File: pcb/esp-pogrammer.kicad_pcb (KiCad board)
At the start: 2 copper layers, 30.2 x 43.7 mm, 31 parts, among them J1 USB_C_Receptacle_USB2.0, J2 TC2030-IDC, Q1 MMDT3904, Q2 MMDT3904, SW1 SW_SPDT, SW2 SW_Push, SW3 SW_Push, U1 CH340G, U2 AMS1117-3.3, Y1 12 MHz

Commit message: updates layout
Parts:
- moved C5 6.84 mm to (88.6, 57.9)
- moved R2 4.63 mm to (90.7, 53.0)
- moved R5 2.57 mm to (74.4, 73.0), turned to -90 degrees
- moved R1 1.74 mm to (93.0, 53.0)
- moved J2 0.30 mm to (93.7, 73.0)
- moved D1 0.20 mm to (80.3, 72.8)
- moved D2 0.20 mm to (80.3, 76.4)
- moved D3 0.20 mm to (80.3, 80.4)
- moved R6 0.20 mm to (85.8, 72.9), turned to 180 degrees
- moved R7 0.20 mm to (85.8, 76.4), turned to 180 degrees
- moved R8 0.20 mm to (85.8, 80.4), turned to 180 degrees
- turned R9 to 0 degrees
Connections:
- C8 pad 2: Net-(C8-Pad2) -> GND
- R5 pad 1: +3V3 -> 3.3V OUT
- SW2 pad 1: Net-(C8-Pad2) -> GND
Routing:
- net TXD: track 0.00 -> 21.7 mm
- net 3.3V OUT: track 0.00 -> 21.4 mm, vias 0 -> 1
- net VBUS: track 0.00 -> 20.6 mm
- net +3V3: track 0.00 -> 20.3 mm, vias 0 -> 3
- net unconnected-(J1-PadS1): track 0.00 -> 17.0 mm
- net RXD: track 0.00 -> 14.3 mm
- net D+: track 0.00 -> 11.0 mm
- net Net-(J1-PadA5): track 0.00 -> 10.4 mm
- net D-: track 0.00 -> 9.77 mm
- net GND: track 0.00 -> 5.66 mm
- net Net-(D1-Pad2): track 0.00 -> 3.93 mm
- net Net-(D3-Pad2): track 0.00 -> 3.91 mm
- net Net-(D2-Pad2): track 0.00 -> 3.89 mm
- net Net-(D4-Pad2): track 0.00 -> 2.29 mm
- net Net-(J1-PadB5): track 0.00 -> 2.16 mm, vias 0 -> 1
- added copper zone on B.Cu, net +3V3
- added copper zone on F.Cu, net GND

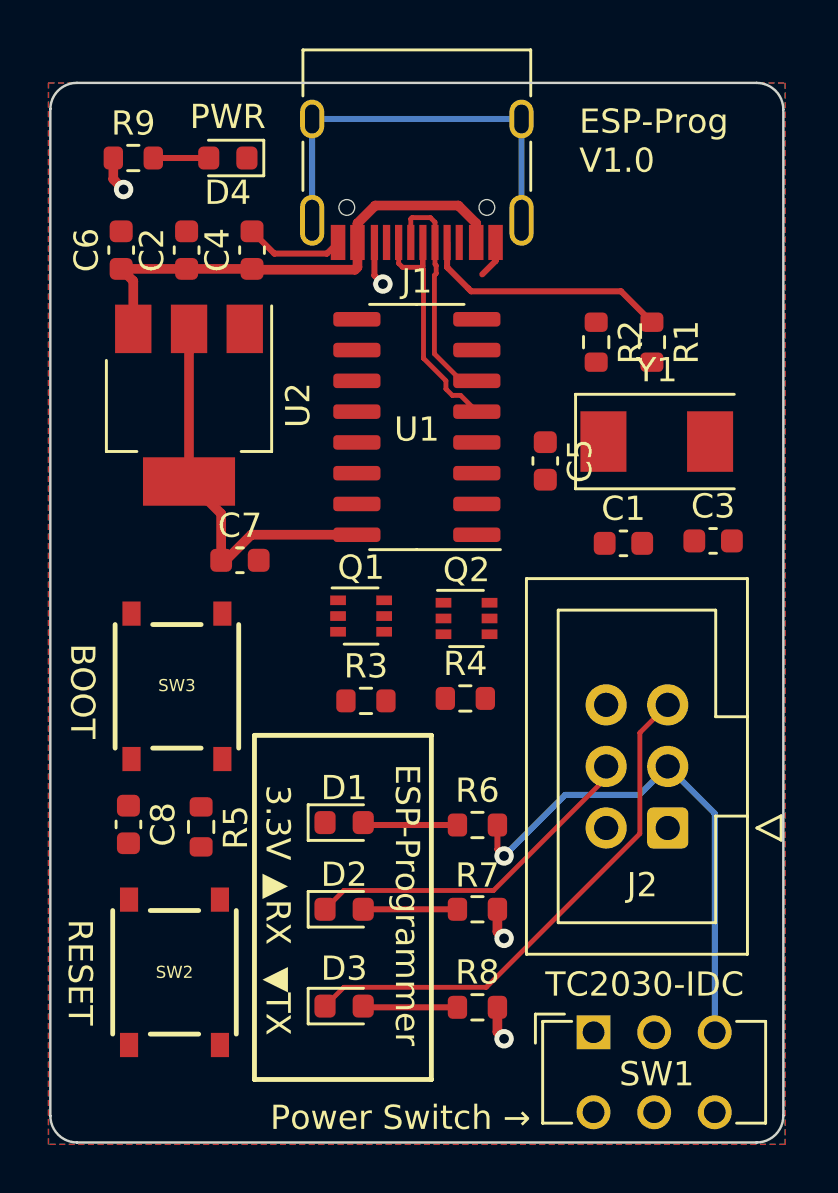
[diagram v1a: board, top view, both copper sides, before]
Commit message: added some filter caps, replaced local chip filter, replaced crystal caps, fixed switched power on reset, routed, rounded.
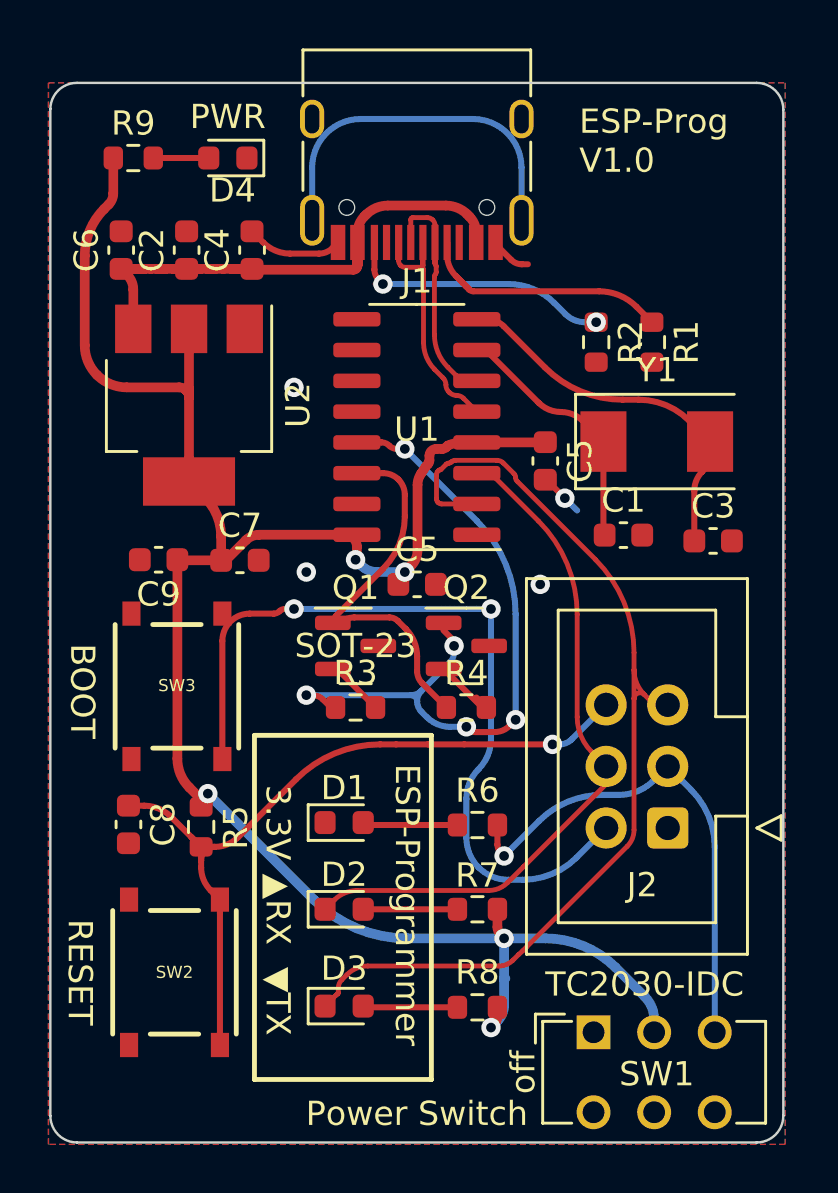
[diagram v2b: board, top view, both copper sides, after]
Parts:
- added C5: 0.1uF, Capacitor_SMD:C_0603_1608Metric, F.Cu at (83.3, 63.0)
- added C9: 10uF, Capacitor_SMD:C_0603_1608Metric, F.Cu at (72.6, 62.0)
- C1, C3: value 10uF -> 22pF
- Q1, Q2: footprint Package_TO_SOT_SMD:SOT-363_SC-70-6 -> Package_TO_SOT_SMD:SOT-23
- moved Q1 1.25 mm to (80.8, 65.5)
- moved Q2 1.13 mm to (85.3, 65.5)
- moved R3 0.51 mm to (80.8, 68.1)
- moved R4 0.37 mm to (85.3, 68.1)
- moved C1 0.34 mm to (91.8, 61.0)
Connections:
- R5 pad 1: 3.3V OUT -> +3V3
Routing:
- net +3V3: track 20.3 -> 85.1 mm, vias 3 -> 5
- net BOOT: track 0.00 -> 33.8 mm, vias 0 -> 2
- net RESET: track 0.00 -> 32.1 mm, vias 0 -> 1
- net DTR: track 0.00 -> 29.9 mm, vias 0 -> 5
- net TXD: track 21.7 -> 41.8 mm
- net RTS: track 0.00 -> 16.1 mm
- net Net-(C3-Pad1): track 0.00 -> 15.5 mm
- net RXD: track 14.3 -> 28.7 mm
- net Net-(C1-Pad1): track 0.00 -> 10.4 mm
- net Net-(J1-PadB5): track 2.16 -> 11.4 mm, vias 1 -> 2
- net Net-(Q2-Pad2): track 0.00 -> 2.90 mm
- net Net-(Q1-Pad2): track 0.00 -> 2.41 mm
- net GND: track 5.66 -> 7.56 mm, vias 0 -> 4
- net unconnected-(J1-PadS1): track 17.0 -> 15.1 mm
- net D+: track 11.0 -> 9.86 mm
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- added copper zone on B.Cu, net GND
- removed copper zone on B.Cu, net +3V3
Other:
- board text added: "Power Switch"
- board text added: "off"
- board text added: "on"
- board text removed: "Power Switch →"

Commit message: fixed transistors. minor changes. ordered prototype 0.1.
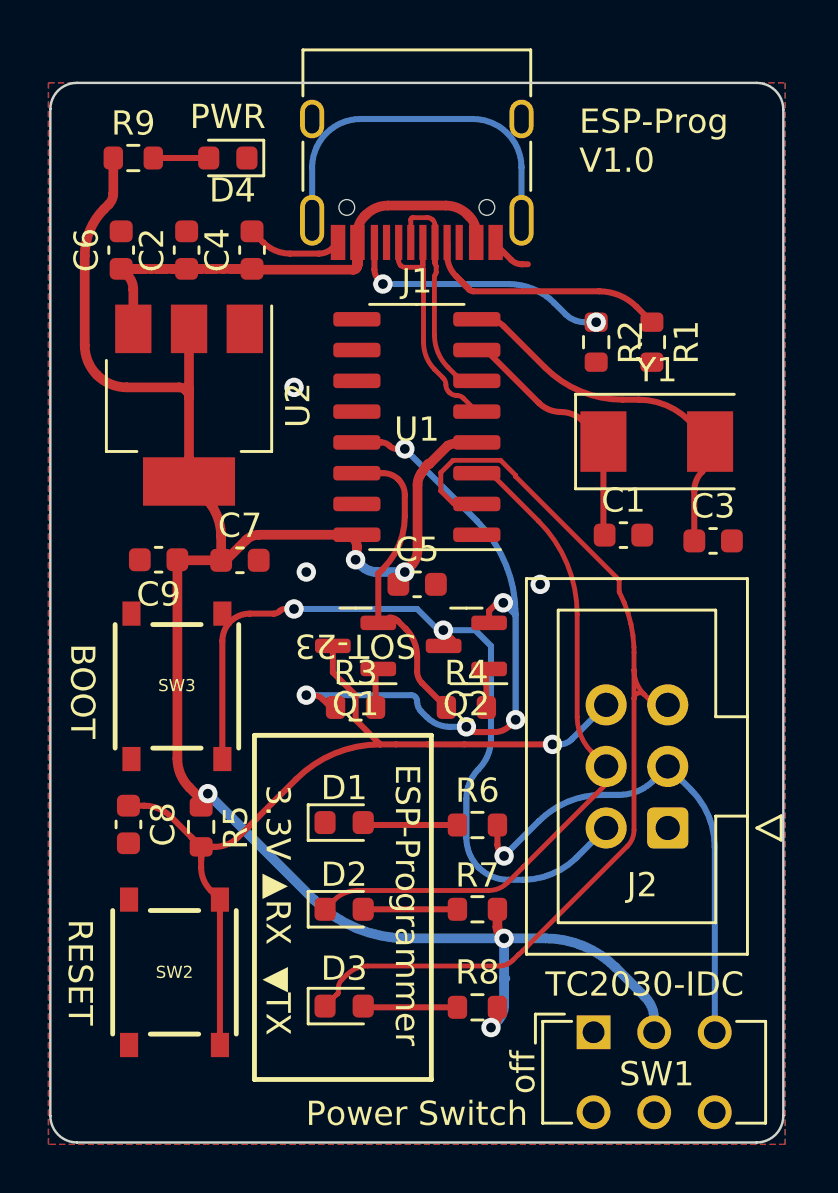
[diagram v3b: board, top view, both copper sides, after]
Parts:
- removed the C5 at (88.6, 57.9)
- Q1, Q2: value MMDT3904 -> S8050
- turned Q1 to 180 degrees
- turned Q2 to 180 degrees
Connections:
- Q1 pad 1: RTS -> Net-(Q1-Pad1)
- Q1 pad 2: Net-(Q1-Pad2) -> RTS
- Q1 pad 3: (no net) -> RESET
- Q2 pad 1: DTR -> Net-(R4-Pad2)
- Q2 pad 2: Net-(Q2-Pad2) -> DTR
- Q2 pad 3: (no net) -> BOOT
- R3 pad 2: Net-(Q1-Pad2) -> Net-(Q1-Pad1)
- R4 pad 2: Net-(Q2-Pad2) -> Net-(R4-Pad2)
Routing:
- net RESET: track 32.1 -> 37.0 mm
- net +3V3: track 85.1 -> 81.5 mm
- net RTS: track 16.1 -> 12.7 mm
- net Net-(Q2-Pad2): track 2.90 -> 0.00 mm
- net Net-(Q1-Pad2): track 2.41 -> 0.00 mm
- net DTR: track 29.9 -> 27.7 mm
- net Net-(R4-Pad2): track 0.00 -> 2.04 mm
- net GND: track 7.56 -> 5.72 mm, vias 4 -> 3
- net Net-(Q1-Pad1): track 0.00 -> 1.64 mm
